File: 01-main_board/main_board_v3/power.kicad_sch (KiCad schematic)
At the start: 24 parts, among them IC1 MAX6105EUR+T, IC11 LT3973EMSE-5#PBF, IC2 LP5907MFX-2.5_NOPB, U4 TPS2115APWR

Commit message: arranged layout fully, traces almost done, planes wip
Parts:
- C61: footprint Capacitor_SMD:C_0402_1005Metric -> Capacitor_SMD:C_0603_1608Metric
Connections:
- net 3V3_esp is gone; now on net 3V3_teensy: C1.1, IC2.1 (IN)
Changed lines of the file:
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@@
 		)
 	)
-	(global_label "3V3_esp"
+	(global_label "3V3_teensy"
 		(shape input)
 		(at 115.57 71.12 180)
@@
 		)
 		(property "Intersheetrefs" "${INTERSHEET_REFS}"
-			(at 104.8439 71.12 0)
+			(at 102.062 71.12 0)
 			(effects
 				(font
@@
 			)
 		)
-		(property "Footprint" "Capacitor_SMD:C_0402_1005Metric"
+		(property "Footprint" "Capacitor_SMD:C_0603_1608Metric"
 			(at 93.98 102.87 0)
 			(effects

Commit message: finished layout
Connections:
- net 3V3_teensy renamed 3V3_esp
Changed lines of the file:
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@@
 		)
 	)
-	(global_label "3V3_teensy"
+	(global_label "3V3_esp"
 		(shape input)
 		(at 115.57 71.12 180)
@@
 		)
 		(property "Intersheetrefs" "${INTERSHEET_REFS}"
-			(at 102.062 71.12 0)
+			(at 104.8439 71.12 0)
 			(effects
 				(font
@@
 		)
 	)
-	(global_label "3V3_teensy"
+	(global_label "3V3_esp"
 		(shape input)
 		(at 127 76.2 270)
@@
 		)
 		(property "Intersheetrefs" "${INTERSHEET_REFS}"
-			(at 127 89.708 90)
+			(at 127 86.9261 90)
 			(effects
 				(font

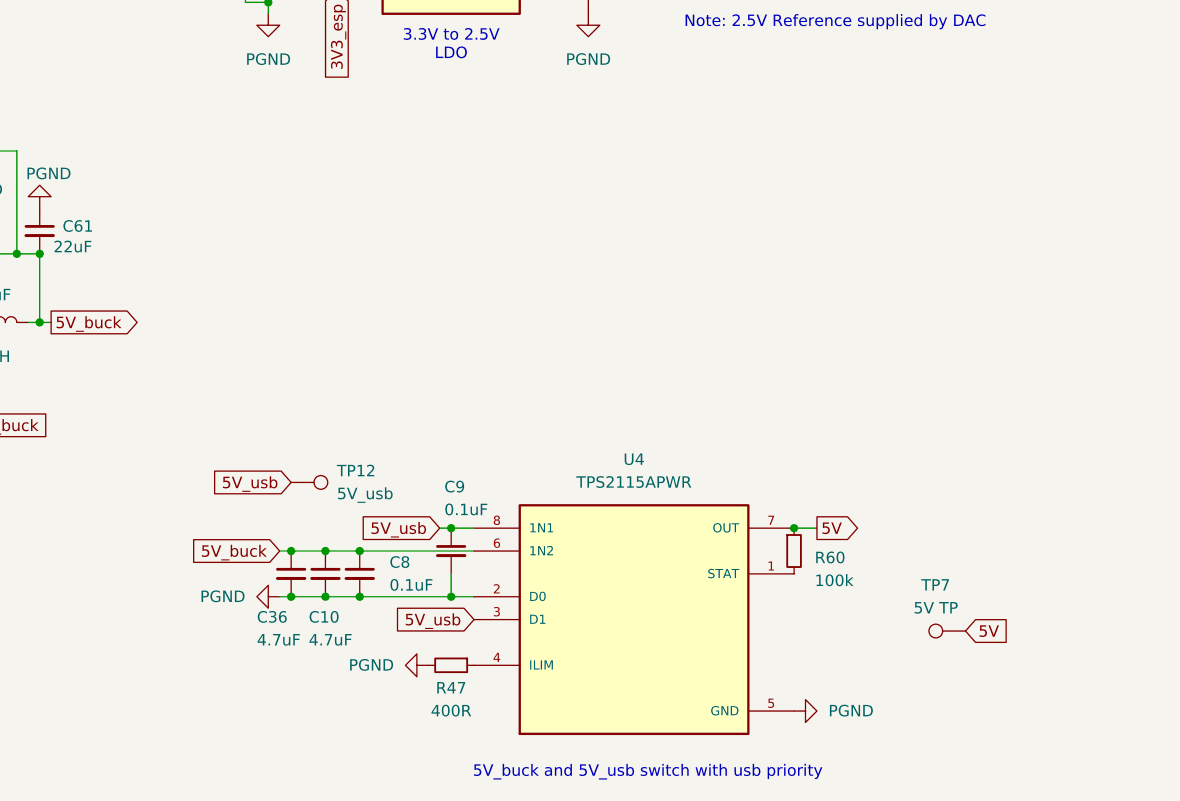
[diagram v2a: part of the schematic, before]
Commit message: added high speed signal gnd plane, updated fpc connectors
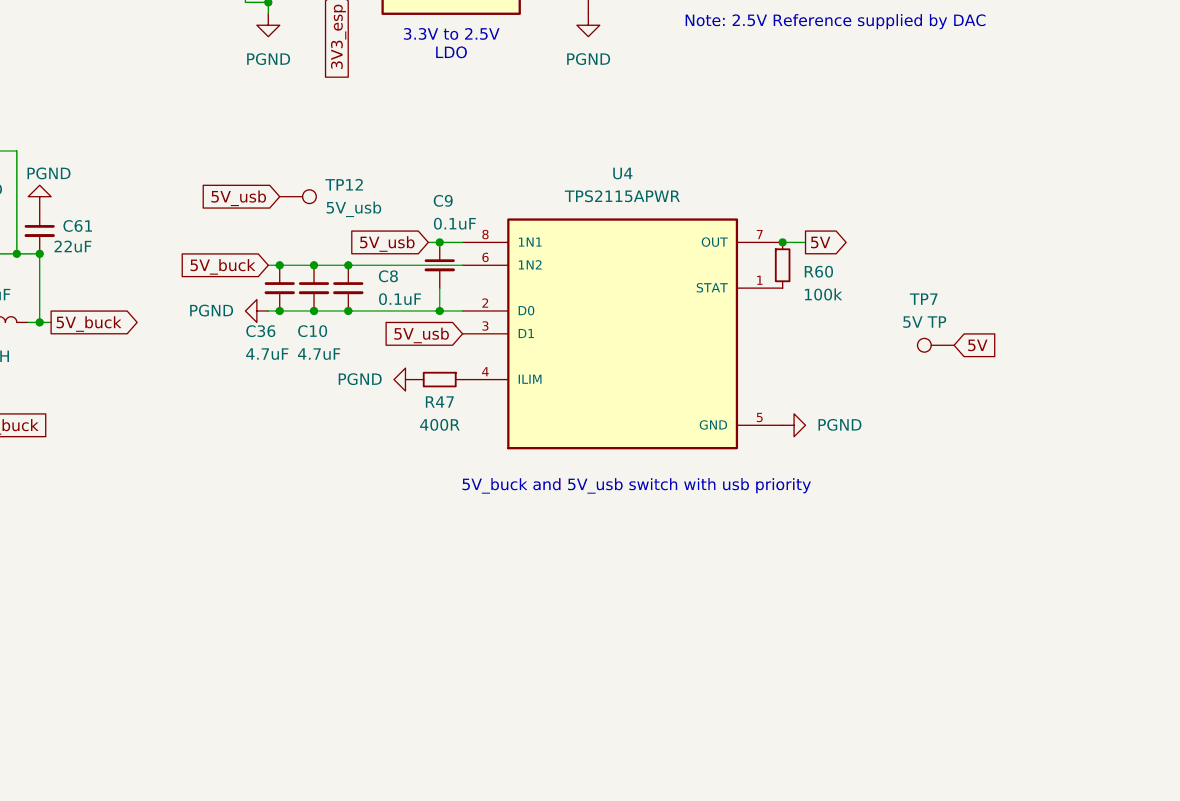
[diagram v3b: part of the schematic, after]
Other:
- moved on the sheet: C10, C36, C8, C9, R47, R60, TP12, TP7, U4
